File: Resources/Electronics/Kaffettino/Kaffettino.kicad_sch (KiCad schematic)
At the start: 53 parts, among them J1 PPTC101LFBN-RC, J2 OSTVN02A150, J3 OSTVN04A150, J5 OSTVN04A150, M1 RFID-RC522, U1 PCF8574AN, U2 ESP32-38Pin-Wroom, U3 DFR0299

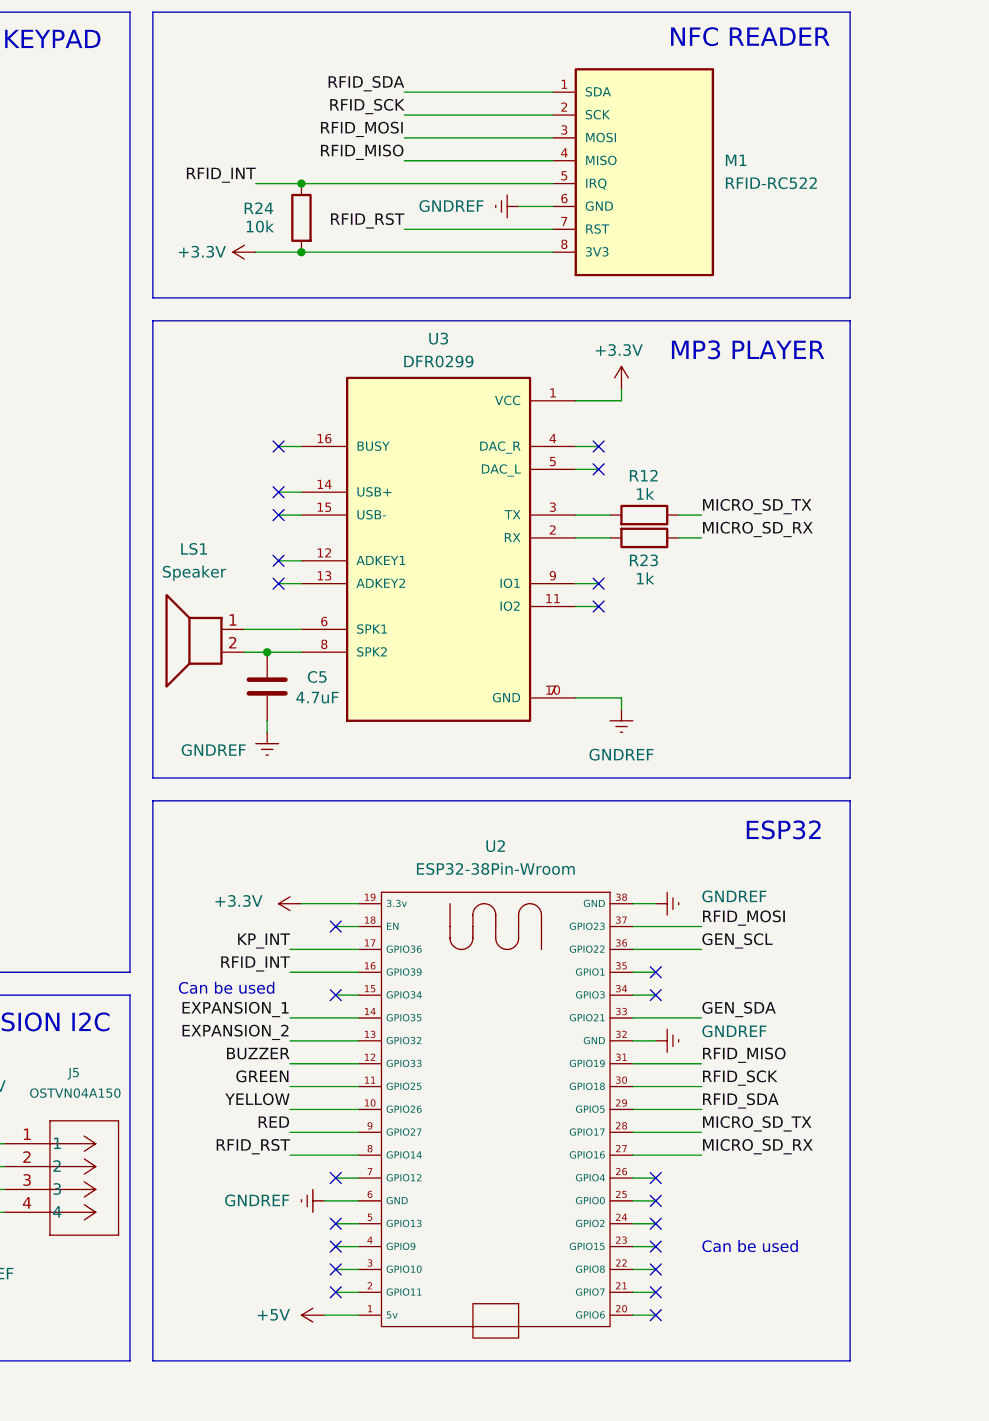
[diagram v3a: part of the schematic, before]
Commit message: Embedded: Completed integration of the sensors and boards. Now will start implementation
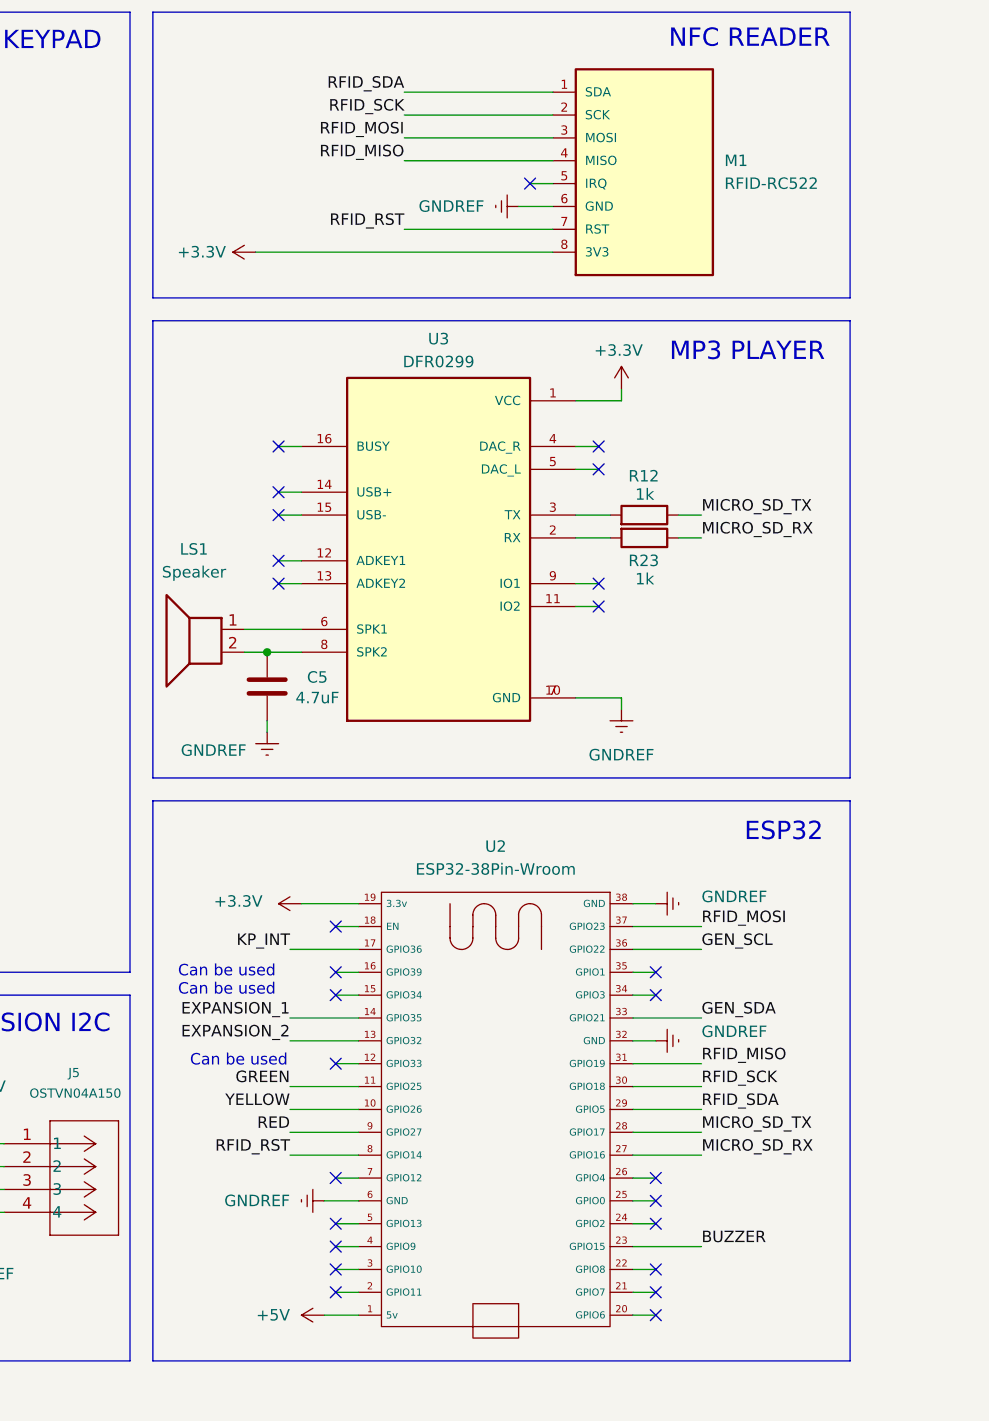
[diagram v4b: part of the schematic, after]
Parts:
- removed R24: 10k, Resistor_THT:R_Axial_DIN0207_L6.3mm_D2.5mm_P10.16mm_Horizontal, symbol Device:R
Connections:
- net BUZZER: now also U2.23 (GPIO15); no longer U2.12 (GPIO33)
- net RFID_INT: no longer names the net of M1.5 (IRQ)
- net RFID_INT: no longer U2.16 (GPIO39)
- no-connect marks 27 -> 29
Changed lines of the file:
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@@
 		)
 	)
+	(text "Can be used"
+		(exclude_from_sim no)
+		(at 208.534 120.65 0)
+		(effects
+			(font
+				(size 1.27 1.27)
+			)
+			(justify left)
+		)
+	)
+	(text "Can be used"
+		(exclude_from_sim no)
+		(at 220.726 130.556 0)
+		(effects
+			(font
+				(size 1.27 1.27)
+			)
+			(justify right)
+		)
+	)
 	(text "EXPANSION PINS"
 		(exclude_from_sim no)
@@
 	(text "Can be used"
 		(exclude_from_sim no)
-		(at 266.7 151.384 0)
-		(effects
-			(font
-				(size 1.27 1.27)
-			)
-			(justify left)
-		)
-	)
-	(text "Can be used"
-		(exclude_from_sim no)
 		(at 208.534 122.682 0)
 		(effects
@@
 	)
 	(junction
-		(at 222.25 40.64)
-		(diameter 0)
-		(color 0 0 0 0)
-	)
-	(junction
 		(at 115.57 43.18)
 		(diameter 0)
@@
 		(color 0 0 0 0)
 	)
-	(junction
-		(at 222.25 33.02)
-		(diameter 0)
-		(color 0 0 0 0)
-	)
 	(no_connect
 		(at 226.06 123.19)
@@
 	)
 	(no_connect
-		(at 261.62 151.13)
+		(at 226.06 148.59)
 	)
 	(no_connect
-		(at 226.06 148.59)
+		(at 226.06 120.65)
 	)
 	(no_connect
@@
 	)
 	(no_connect
+		(at 226.06 130.81)
+	)
+	(no_connect
 		(at 261.62 143.51)
 	)
@@
 	)
 	(no_connect
+		(at 247.65 33.02)
+	)
+	(no_connect
 		(at 219.71 77.47)
 	)
@@
 	(wire
 		(pts
-			(xy 217.17 33.02) (xy 222.25 33.02)
-		)
-		(stroke
-			(width 0)
-			(type default)
-		)
-	)
-	(wire
-		(pts
 			(xy 33.02 43.18) (xy 40.64 43.18)
 		)
@@
 			(width 0)
 			(type default)
-			(color 0 0 0 1)
 		)
 	)
@@
 	(wire
 		(pts
-			(xy 228.6 130.81) (xy 220.98 130.81)
+			(xy 259.08 151.13) (xy 266.7 151.13)
 		)
 		(stroke
 			(width 0)
 			(type default)
-			(color 0 0 0 1)
 		)
 	)
@@
 	(wire
 		(pts
-			(xy 220.98 120.65) (xy 228.6 120.65)
-		)
-		(stroke
-			(width 0)
-			(type default)
-		)
-	)
-	(wire
-		(pts
 			(xy 167.64 101.6) (xy 167.64 104.14)
 		)
@@
 	(wire
 		(pts
-			(xy 217.17 40.64) (xy 222.25 40.64)
+			(xy 217.17 40.64) (xy 250.19 40.64)
 		)
 		(stroke
@@
 	(wire
 		(pts
+			(xy 247.65 33.02) (xy 250.19 33.02)
+		)
+		(stroke
+			(width 0)
+			(type default)
+		)
+	)
+	(wire
+		(pts
 			(xy 69.85 72.39) (xy 69.85 71.12)
 		)
@@
 	(wire
 		(pts
+			(xy 226.06 130.81) (xy 228.6 130.81)
+		)
+		(stroke
+			(width 0)
+			(type default)
+		)
+	)
+	(wire
+		(pts
 			(xy 43.18 181.61) (xy 43.18 184.15)
 		)
@@
 	(wire
 		(pts
-			(xy 222.25 33.02) (xy 250.19 33.02)
-		)
-		(stroke
-			(width 0)
-			(type default)
-		)
-	)
-	(wire
-		(pts
 			(xy 53.34 20.32) (xy 53.34 27.94)
 		)
@@
 	(wire
 		(pts
-			(xy 115.57 93.98) (xy 124.46 93.98)
+			(xy 226.06 120.65) (xy 228.6 120.65)
 		)
 		(stroke
@@
 	(wire
 		(pts
-			(xy 55.88 160.02) (xy 55.88 163.83)
+			(xy 115.57 93.98) (xy 124.46 93.98)
 		)
 		(stroke
 			(width 0)
 			(type default)
-			(color 255 0 0 1)
 		)
 	)
 	(wire
 		(pts
-			(xy 261.62 151.13) (xy 259.08 151.13)
+			(xy 55.88 160.02) (xy 55.88 163.83)
 		)
 		(stroke
 			(width 0)
 			(type default)
+			(color 255 0 0 1)
 		)
 	)
@@
 	(wire
 		(pts
-			(xy 222.25 40.64) (xy 250.19 40.64)
-		)
-		(stroke
-			(width 0)
-			(type default)
-		)
-	)
-	(wire
-		(pts
 			(xy 157.48 101.6) (xy 157.48 104.14)
 		)
@@
 		)
 	)
-	(label "RFID_INT"
-		(at 217.17 33.02 180)
-		(effects
-			(font
-				(size 1.27 1.27)
-			)
-			(justify right bottom)
-		)
-	)
 	(label "RFID_SCK"
 		(at 233.68 25.4 180)
@@
 	)
 	(label "BUZZER"
-		(at 220.98 130.81 180)
+		(at 266.7 151.13 0)
 		(effects
 			(font
@@
 				(color 0 0 0 1)
 			)
-			(justify right bottom)
+			(justify left bottom)
 		)
 	)
@@
 		)
 	)
-	(label "RFID_INT"
-		(at 220.98 120.65 180)
-		(effects
-			(font
-				(size 1.27 1.27)
-			)
-			(justify right bottom)
-		)
-	)
 	(label "RFID_RST"
 		(at 233.68 38.1 180)
@@
 					(unit 1)
 				)
-			)
-		)
-	)
-	(symbol
-		(lib_id "Device:R")
-		(at 222.25 36.83 0)
-		(mirror y)
-		(unit 1)
-		(exclude_from_sim no)
-		(in_bom yes)
-		(on_board yes)
-		(dnp no)
-		(property "Reference" "R24"
-			(at 219.202 35.814 0)
-			(effects
-				(font
-					(size 1.27 1.27)
-				)
-				(justify left)
-			)
-		)
-		(property "Value" "10k"
-			(at 219.202 37.846 0)
-			(effects
-				(font
-					(size 1.27 1.27)
-				)
-				(justify left)
-			)
-		)
-		(property "Footprint" "Resistor_THT:R_Axial_DIN0207_L6.3mm_D2.5mm_P10.16mm_Horizontal"
-			(at 224.028 36.83 90)
-			(effects
-				(font
-					(size 1.27 1.27)
-				)
-				(hide yes)
-			)
-		)
-		(property "Datasheet" "~"
-			(at 222.25 36.83 0)
-			(effects
-				(font
-					(size 1.27 1.27)
-				)
-				(hide yes)
-			)
-		)
-		(property "Description" "Resistor"
-			(at 222.25 36.83 0)
-			(effects
-				(font
-					(size 1.27 1.27)
-				)
-				(hide yes)
-			)
-		)
-		(pin "2"
-		)
-		(pin "1"
-		)
-		(instances
-			(project "Kaffettino"
-				(path "/5e636569-7bbd-43ff-bd8f-9986b616afcc"
-					(reference "R24")
-					(unit 1)
-				)

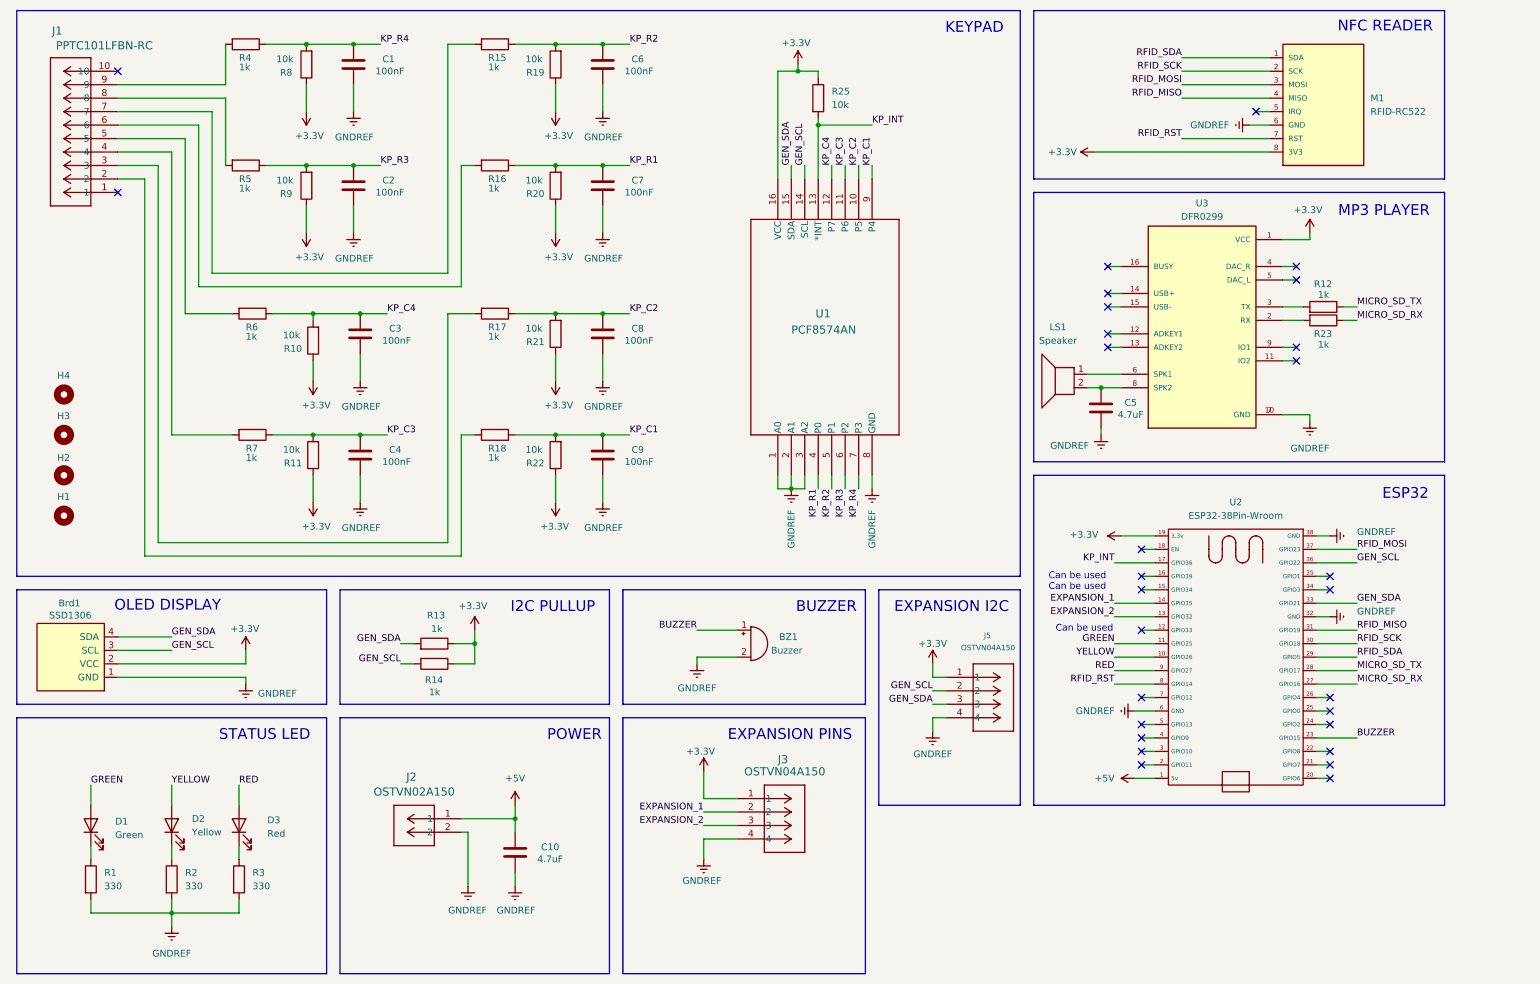
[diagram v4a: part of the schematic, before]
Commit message: Trying images on display and almost finished PCB design.
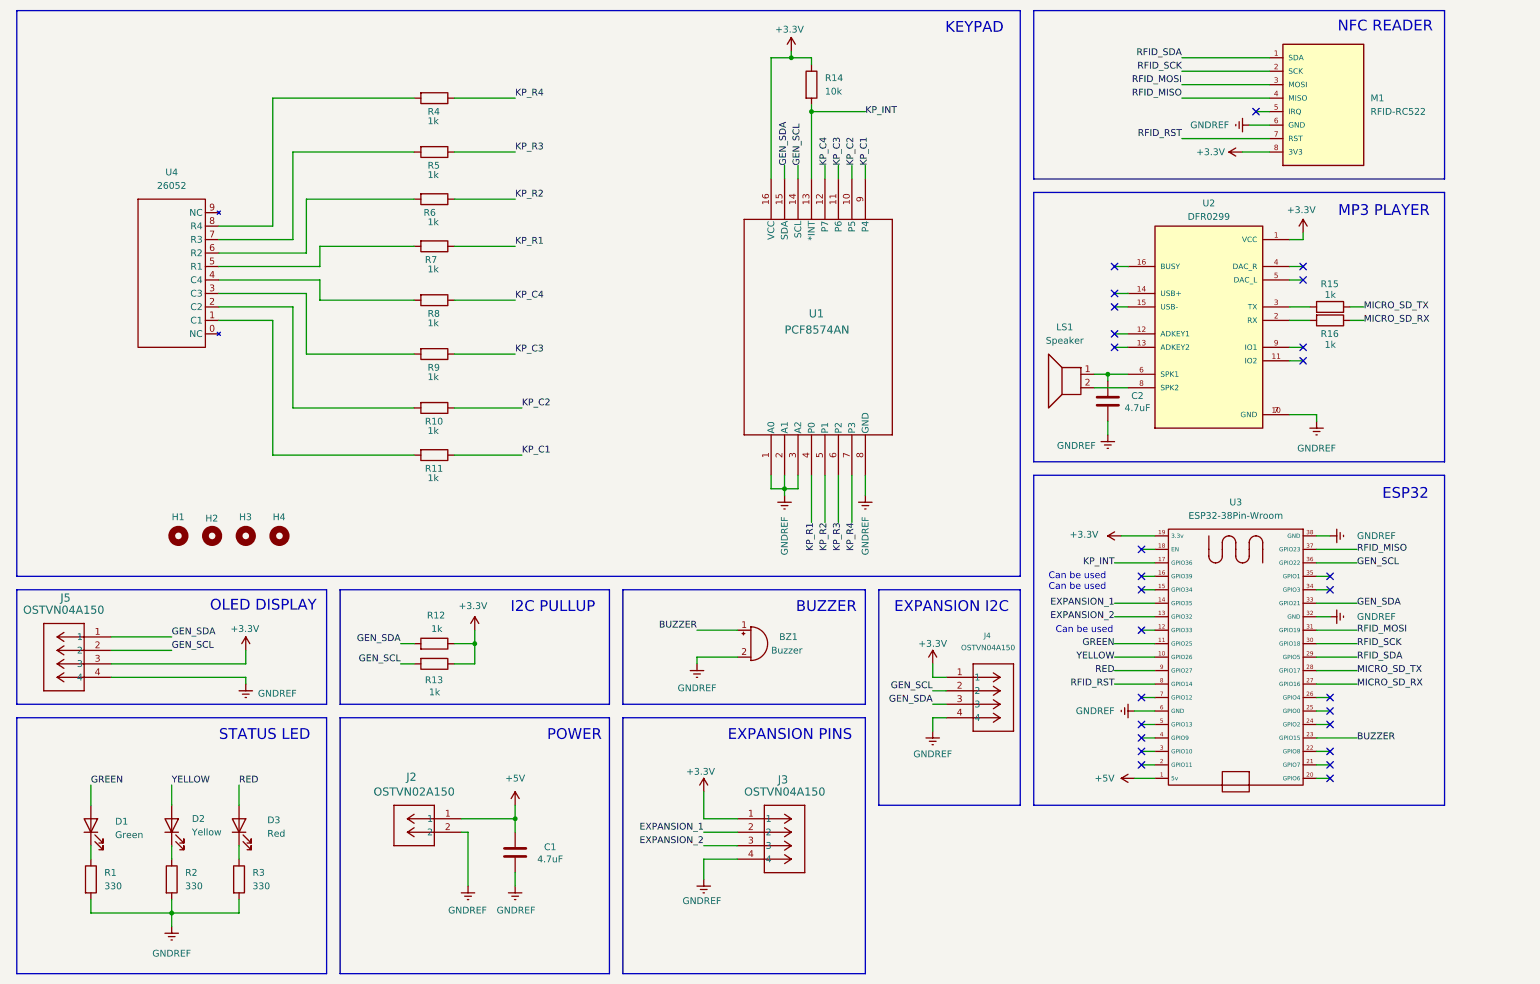
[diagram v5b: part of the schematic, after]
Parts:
- removed Brd1: SSD1306, Display:Adafruit_SSD1306, symbol SSD1306-128x64_OLED:SSD1306
- removed C1, C2, C3, C4, C6, C7, C8, C9: 100nF, Capacitor_THT:C_Disc_D3.0mm_W1.6mm_P2.50mm, symbol Device:C
- removed J1: PPTC101LFBN-RC, PPTC101LFBN_RC:CONN10_101LFBN-RC_SUL, symbol PPTC101LFBN_RC:PPTC101LFBN-RC
- removed R10, R11, R19, R20, R21, R22, R8, R9: 10k, Resistor_THT:R_Axial_DIN0207_L6.3mm_D2.5mm_P10.16mm_Horizontal, symbol Device:R
- added J5: OSTVN04A150, OSTVN04A150:CONN_OSTVN04A150_OST, symbol 2025-11-13_14-58-24:OSTVN04A150
- added U4: 26052, 26052 matrix keypad 4x4:26052 matrix keypad 4x4, symbol 26052:26052_matrix_keypad_4x4
- renumbered C10 to C1, C5 to C2, J5 to J4, R17 to R10, R18 to R11, R13 to R12, R14 to R13, R25 to R14, R12 to R15, R23 to R16, R15 to R6, R16 to R7, R6 to R8, R7 to R9, U3 to U2, U2 to U3
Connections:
- net +3.3V: now also J5.3
- net GEN_SCL: now also J5.2
- net GEN_SDA: now also J5.1
- net GNDREF: now also J5.4
- net RFID_MISO: now also U3.37 (GPIO23); no longer U3.31 (GPIO19)
- net RFID_MOSI: now also U3.31 (GPIO19); no longer U3.37 (GPIO23)
- net at R9.2: now also U4.3 (C3)
- net at R6.2: now also U4.6 (R2)
- net at LS1.1, U2.6 (SPK1): now also C2.1
- net at LS1.2, U2.8 (SPK2): no longer C2.1
- net at R5.2: now also U4.7 (R3)
- net at R10.2: now also U4.2 (C2)
- net at R7.2: now also U4.5 (R1)
- net at R8.2: now also U4.4 (C4)
- net at R11.2: now also U4.1 (C1)
- net at R4.2: now also U4.8 (R4)
- no-connect marks 29 -> 27
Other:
- moved on the sheet: C2, H1, H2, H3, H4, J3, LS1, R10, R11, R14, R15, R16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

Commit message: Finished routing in PCB, waiting for approval
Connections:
- net RFID_MISO: now also U3.31 (GPIO19); no longer U3.37 (GPIO23)
- net RFID_MOSI: now also U3.37 (GPIO23); no longer U3.31 (GPIO19)
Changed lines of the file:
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@@
+		)
+	)
+	(label "RFID_MISO"
+		(at 266.7 130.81 0)
+		(effects
+			(font
+				(size 1.27 1.27)
+			)
+			(justify left)
 		)
 	)
@@
 		)
 	)
-	(label "RFID_MOSI"
-		(at 266.7 130.81 0)
-		(effects
-			(font
-				(size 1.27 1.27)
-			)
-			(justify left)
-		)
-	)
 	(label "GEN_SCL"
 		(at 161.29 43.18 90)
@@
 		)
 	)
+	(label "RFID_MOSI"
+		(at 266.7 115.57 0)
+		(effects
+			(font
+				(size 1.27 1.27)
+			)
+			(justify left)
+		)
+	)
 	(label "RFID_RST"
 		(at 220.98 140.97 180)
@@
 		)
 	)
-	(label "RFID_MISO"
-		(at 266.7 115.57 0)
-		(effects
-			(font
-				(size 1.27 1.27)
-			)
-			(justify left)
-		)
-	)
